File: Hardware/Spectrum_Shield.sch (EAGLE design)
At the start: 27 parts, among them U1 ARDUINO_R3_SHIELD, U2 MSGEQ7SOIC, U3 MSGEQ7SOIC

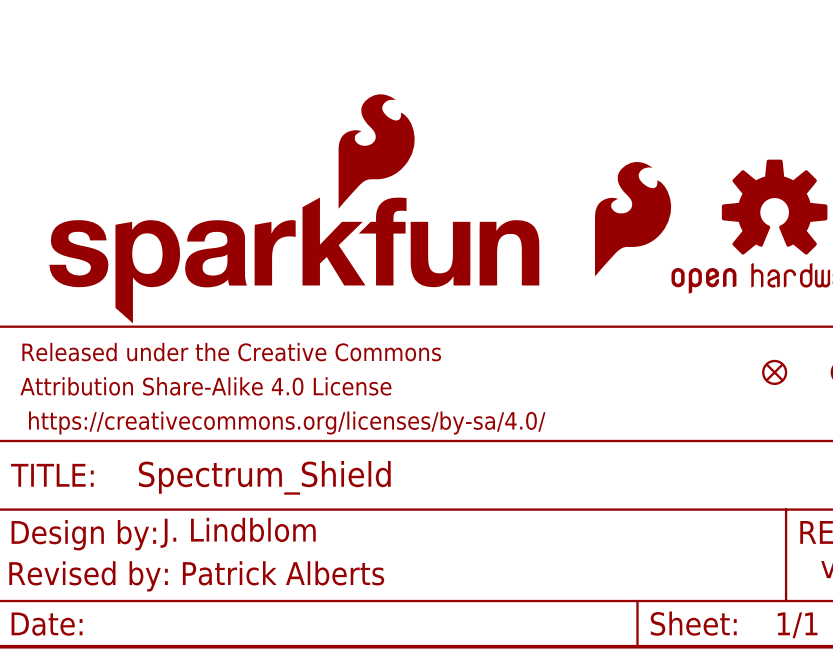
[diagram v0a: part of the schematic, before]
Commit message: Added stand offs, fixed silk.  QC list / attributes
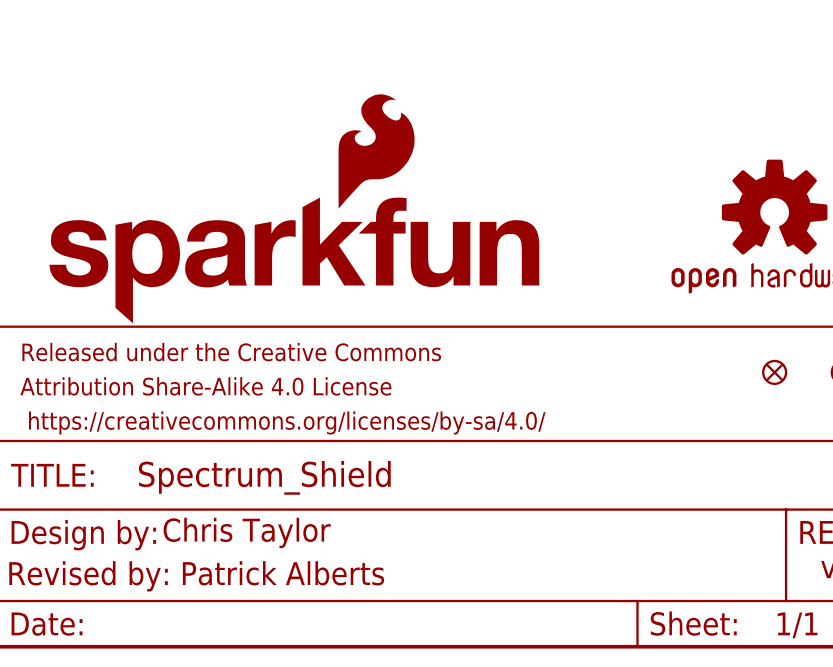
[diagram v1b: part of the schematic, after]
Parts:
- removed LOGO2: SFE_LOGO_FLAME.2_INCH, SparkFun-Aesthetics:SFE_LOGO_FLAME.2_INCH
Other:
- note added: "Chris Taylor"
- note removed: "J. Lindblom"
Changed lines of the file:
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@@
 <?xml version="1.0" encoding="utf-8"?>
 <!DOCTYPE eagle SYSTEM "eagle.dtd">
-<eagle version="7.1.0">
+<eagle version="7.2.0">
 <drawing>
 <settings>
@@
 <part name="AUDIOJACK2" library="SparkFun-Connectors" deviceset="AUDIO-JACK" device="SMD2"/>
 <part name="LOGO1" library="SparkFun-Aesthetics" deviceset="OSHW-LOGO" device="M" value="OSHW-LOGOM"/>
-<part name="LOGO2" library="SparkFun-Aesthetics" deviceset="SFE_LOGO_FLAME" device=".2_INCH" value="SFE_LOGO_FLAME.2_INCH"/>
 <part name="LOGO3" library="SparkFun-Aesthetics" deviceset="SFE_LOGO_NAME_FLAME" device=".1_INCH"/>
 <part name="GND2" library="SparkFun" deviceset="GND" device=""/>
@@
 <text x="224.282" y="131.826" size="1.778" layer="91">for development</text>
 <text x="238.76" y="7.62" size="2.54" layer="94">v16</text>
-<text x="165.608" y="11.684" size="2.54" layer="94">J. Lindblom</text>
+<text x="165.608" y="11.684" size="2.54" layer="94">Chris Taylor</text>
 <text x="148.336" y="6.858" size="2.54" layer="94">Revised by: Patrick Alberts</text>
 <wire x1="0" y1="55.88" x2="119.38" y2="55.88" width="0.2032" layer="97" style="shortdash"/>
@@
 <instance part="U1" gate="G$1" x="175.26" y="137.16"/>
 <instance part="FRAME1" gate="G$1" x="0" y="0"/>
-<instance part="FRAME1" gate="G$2" x="147.32" y="0"/>
+<instance part="FRAME1" gate="V" x="147.32" y="0"/>
 <instance part="R3" gate="G$1" x="152.4" y="119.38" rot="R90"/>
 <instance part="D1" gate="G$1" x="152.4" y="109.22"/>
@@
 <instance part="AUDIOJACK2" gate="G$1" x="109.22" y="43.18" rot="R180"/>
 <instance part="LOGO1" gate="G$1" x="233.68" y="48.26"/>
-<instance part="LOGO2" gate="G$1" x="213.36" y="40.64"/>
 <instance part="LOGO3" gate="G$1" x="152.4" y="35.56"/>
 <instance part="GND2" gate="1" x="93.98" y="35.56"/>

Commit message: Fixed QC Checklist Items
1) Currently there are two 4-way junctions: both below each MSGEQ7
symbol, each 4-way needs to split up into two 3-way junctions.

(2) On the R3 symbol the VCC net crosses over the RESET net. It would be
nice to reorganize these nets to eliminate the intersection all
together.

(3) The Audio jacks are currently named Audiojack1 and 2, these should
have a name that uses the proper connector prefix (JPx) x being a number

(4) Two vias have tStop and bStop polygons set over them: the first is
right next to the OSHW silk, and the other is below U2 (the upper MSGEQ7
IC). These are not used for testing

(5) Audio jacks need a name and value in BRD

(6) Need measures that include the standoffs

(7) As of now the name of the product is not on the board; the previous
rev was without a silk for the product name as well (figured I would
bring it up). Also, it would be nice to get an SFE flame on the top of
the board, like the previous rev.

that's it
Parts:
- added LOGO2: SFE_LOGO_FLAME.2_INCH, SparkFun-Aesthetics:SFE_LOGO_FLAME.2_INCH
- JP1, JP6: value (none) -> 3.5mm Audio Jack
- renumbered AUDIOJACK1 to JP1, AUDIOJACK2 to JP6
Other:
- moved on the sheet: D1, R3, S1
